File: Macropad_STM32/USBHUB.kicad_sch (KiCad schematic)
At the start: 14 parts, among them U2 CY7C65632-28LTXCT, U4 USBLC6-2SC6, Y1 12MHz

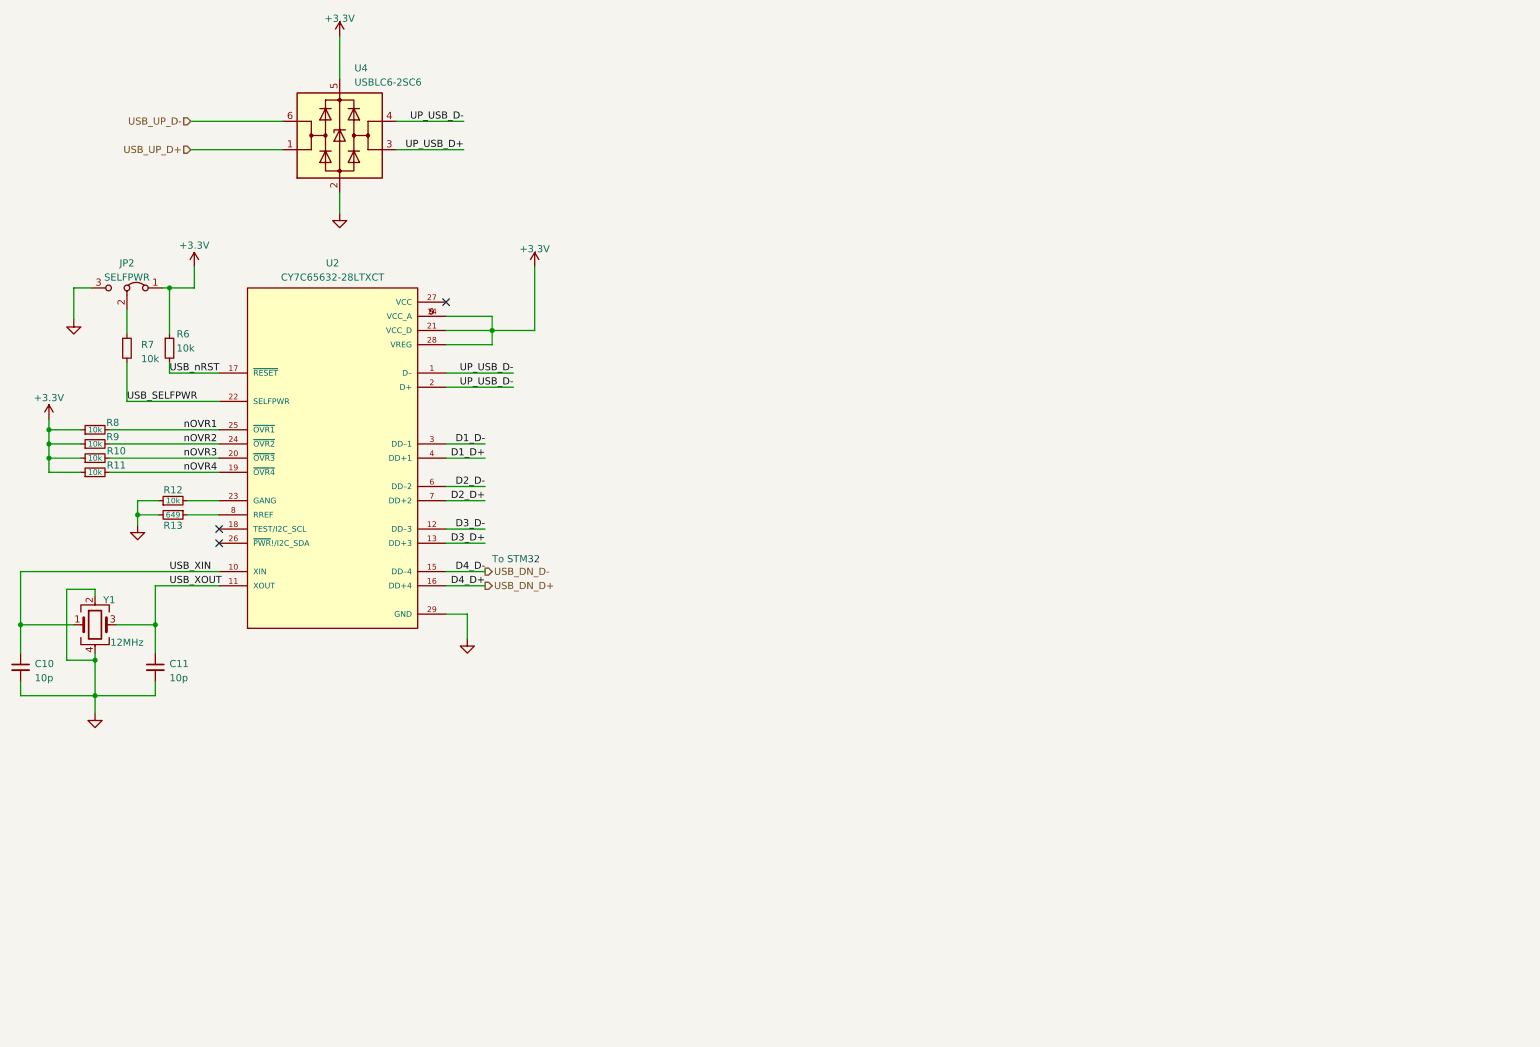
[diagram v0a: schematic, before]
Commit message: USB Hub & Jtag connectors added Todo: - Keypad matrix - Rotary encoders - PCB
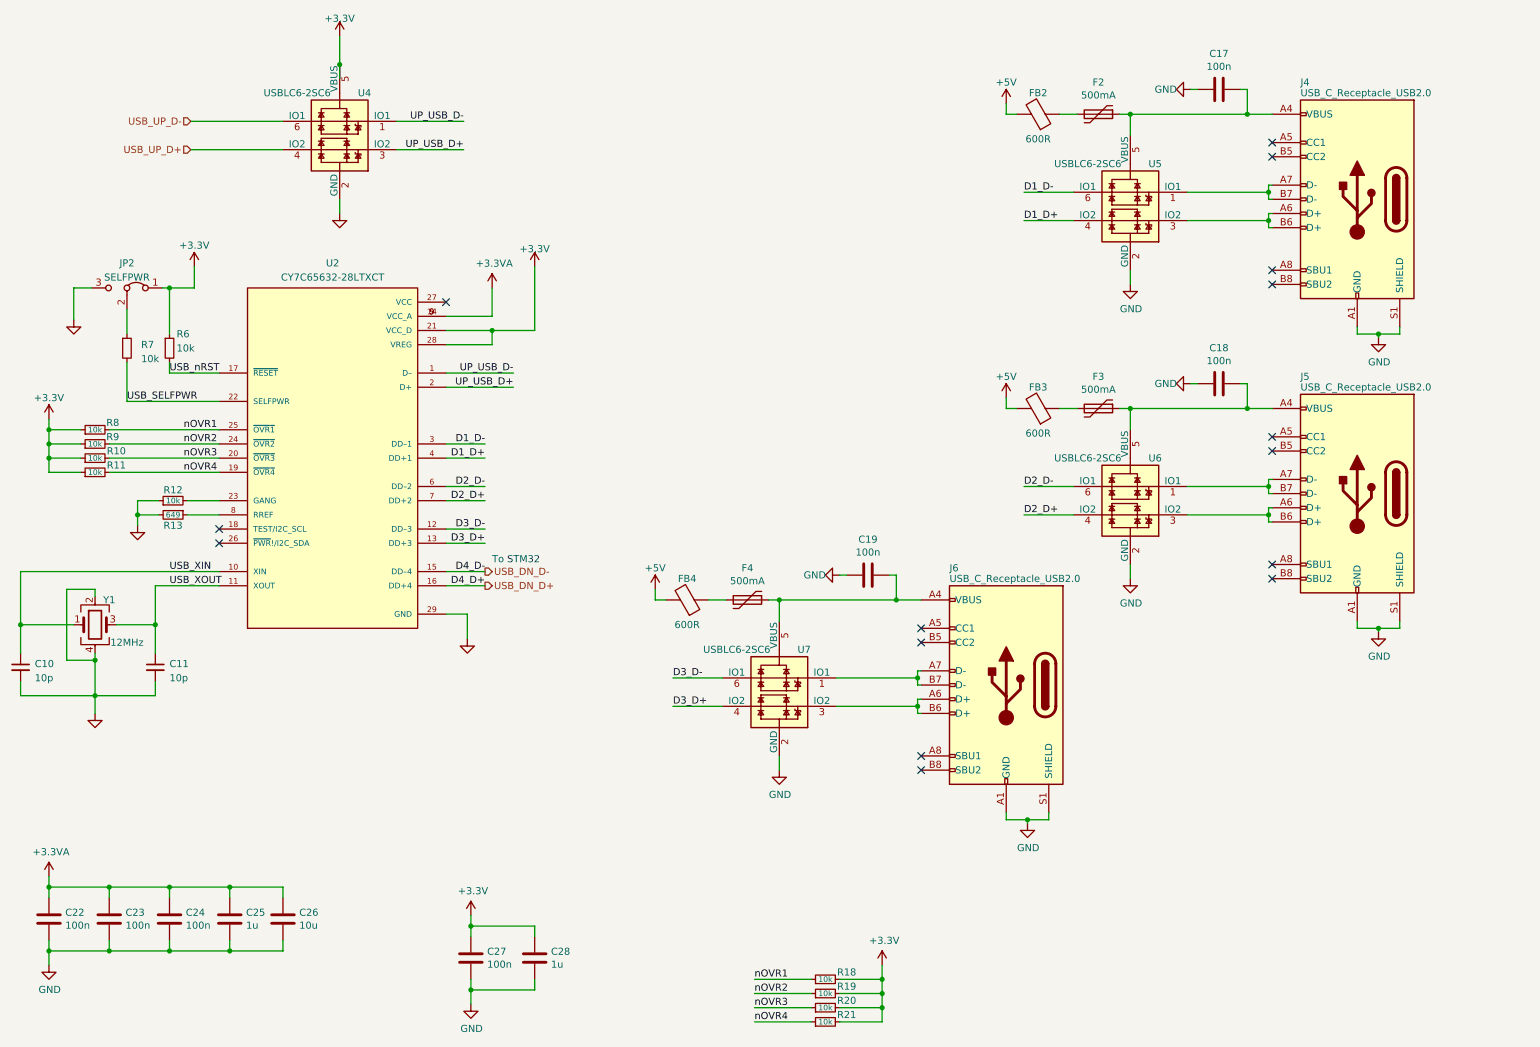
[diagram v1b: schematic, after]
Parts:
- removed U4: USBLC6-2SC6, Package_TO_SOT_SMD:SOT-23-6, symbol Power_Protection:USBLC6-2SC6
- added C17, C18, C19, C22, C23, C24, C27: 100n, Capacitor_SMD:C_0603_1608Metric, symbol Device:C
- added C25, C28: 1u, Capacitor_SMD:C_0603_1608Metric, symbol Device:C
- added C26: 10u, Capacitor_SMD:C_0603_1608Metric, symbol Device:C
- added F2, F3, F4: 500mA, josh-passives-smt:Fuse_0805_2012Metric, symbol Device:Polyfuse
- added FB2, FB3, FB4: 600R, josh-passives-smt:Ferrite_Bead_0603, symbol Hub16-rescue:Ferrite_Bead_PWR-josh-passive
- added J4, J5, J6: USB_C_Receptacle_USB2.0, Connector_USB:USB_C_Receptacle_HRO_TYPE-C-31-M-12, symbol Hub16-rescue:USB_C_Receptacle_USB2.0-Connector
- added R18, R19, R20, R21: 10k, symbol Device:R_Small
- added U4, U5, U6, U7: USBLC6-2SC6, Package_TO_SOT_SMD:SOT-23-6, symbol Hub16-rescue:USBLC6-2SC6-josh-ic
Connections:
- net +3.3V: now also U4.5 (VBUS); no longer U2.14 (VCC_A), U2.5 (VCC_A), U2.9 (VCC_A)
- net D1_D+: now also U5.4 (IO2)
- net D1_D-: now also U5.6 (IO1)
- net D2_D+: now also U6.4 (IO2)
- net D2_D-: now also U6.6 (IO1)
- net D3_D+: now also U7.4 (IO2)
- net D3_D-: now also U7.6 (IO1)
- net GND: now also C17.2, C18.2, C19.2, C22.2, C23.2, C24.2, C25.2, C26.2, C27.2, C28.2, J4.A1 (GND), J4.A12 (GND), J4.B1 (GND), J4.B12 (GND), J4.S1 (SHIELD), J5.A1 (GND), J5.A12 (GND), J5.B1 (GND), J5.B12 (GND), J5.S1 (SHIELD), J6.A1 (GND), J6.A12 (GND), J6.B1 (GND), J6.B12 (GND), J6.S1 (SHIELD), U4.2 (GND), U5.2 (GND), U6.2 (GND), U7.2 (GND)
- net UP_USB_D+: now also U2.2 (D+), U4.3 (IO2)
- net UP_USB_D-: now also U4.1 (IO1); no longer U2.2 (D+)
- net USB_UP_D+: now also U4.4 (IO2)
- net USB_UP_D-: now also U4.6 (IO1)
- net nOVR1: now also R18.1
- net nOVR2: now also R19.1
- net nOVR3: now also R20.1
- net nOVR4: now also R21.1
- new net: F4.2, FB4.1
- new net: C19.1, F4.1, J6.A4 (VBUS), J6.A9 (VBUS), J6.B4 (VBUS), J6.B9 (VBUS), U7.5 (VBUS)
- new net: F2.2, FB2.1
- new net: F3.2, FB3.1
- new net: J5.A7 (D-), J5.B7 (D-), U6.1 (IO1)
- new net: J5.A6 (D+), J5.B6 (D+), U6.3 (IO2)
- new net: C18.1, F3.1, J5.A4 (VBUS), J5.A9 (VBUS), J5.B4 (VBUS), J5.B9 (VBUS), U6.5 (VBUS)
- new net: C17.1, F2.1, J4.A4 (VBUS), J4.A9 (VBUS), J4.B4 (VBUS), J4.B9 (VBUS), U5.5 (VBUS)
- new net: J6.A6 (D+), J6.B6 (D+), U7.3 (IO2)
- new net: J6.A7 (D-), J6.B7 (D-), U7.1 (IO1)
- new net: J4.A7 (D-), J4.B7 (D-), U5.1 (IO1)
- new net: J4.A6 (D+), J4.B6 (D+), U5.3 (IO2)
- new net +3.3VA: C22.1, C23.1, C24.1, C25.1, C26.1, U2.14 (VCC_A), U2.5 (VCC_A), U2.9 (VCC_A)
- new net +3V3: C27.1, C28.1, R18.2, R19.2, R20.2, R21.2
- new net +5V: FB2.2, FB3.2, FB4.2
- no-connect marks 3 -> 15

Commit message: Finished main schematic (excl. matrix)
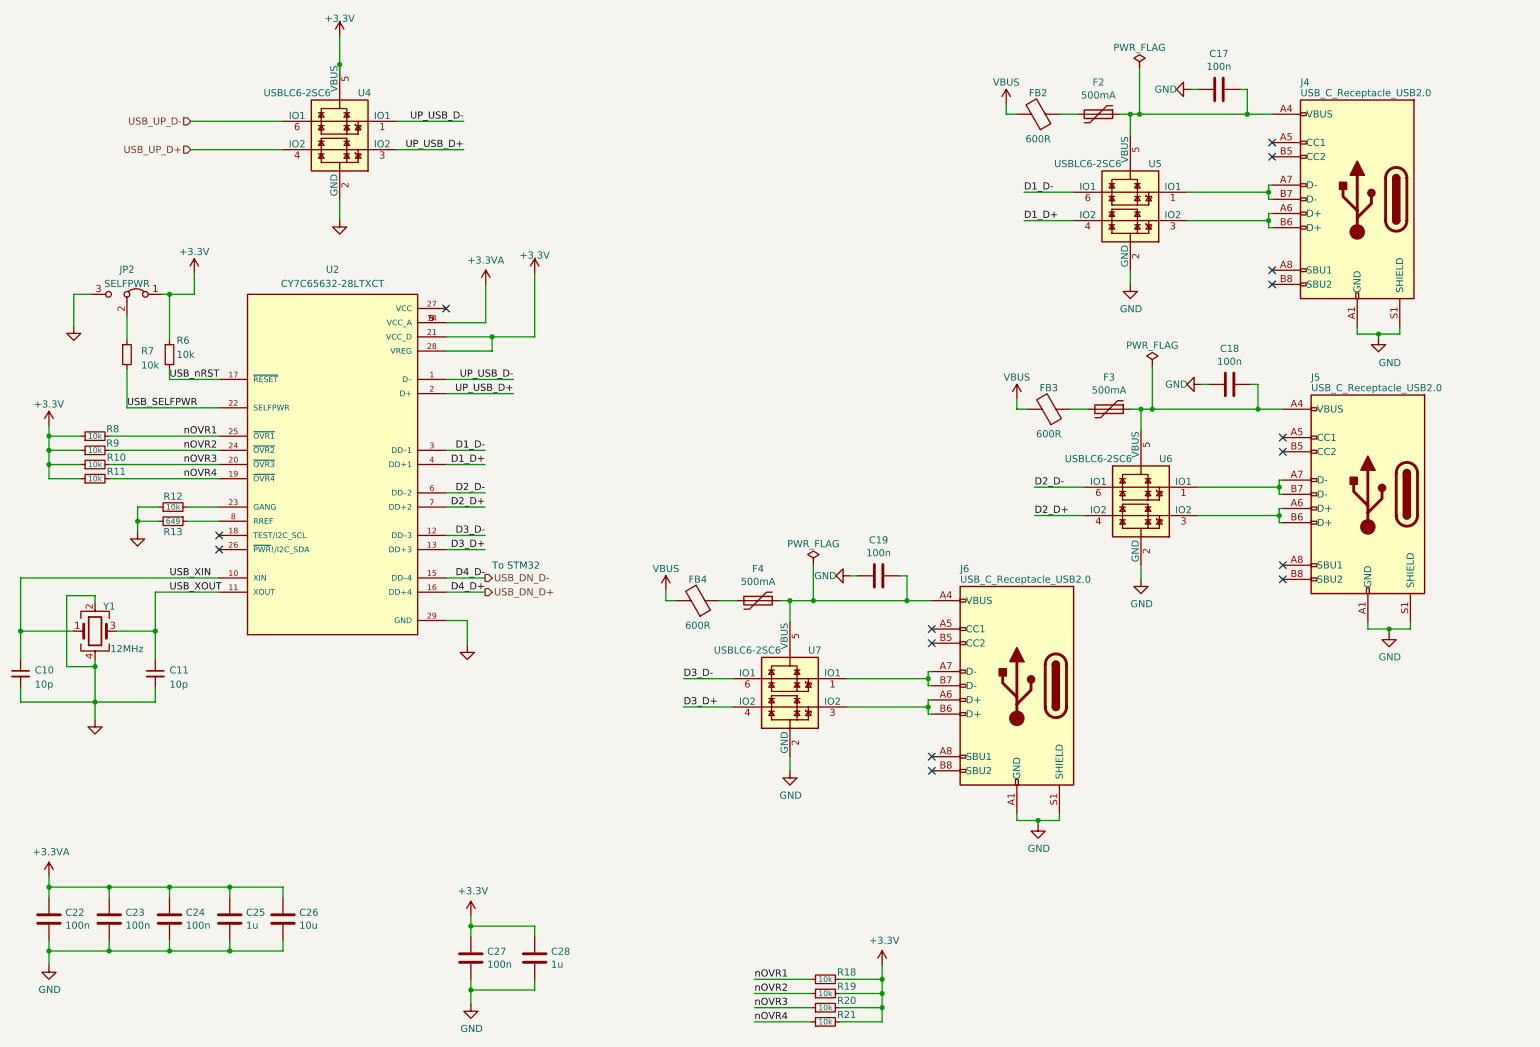
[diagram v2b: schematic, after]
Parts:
- C10, C11: footprint (none) -> Capacitor_SMD:C_0805_2012Metric_Pad1.18x1.45mm_HandSolder
- C17, C18, C19, C22, C23, C24, C25, C26, C27, C28: footprint Capacitor_SMD:C_0603_1608Metric -> Capacitor_SMD:C_0805_2012Metric_Pad1.18x1.45mm_HandSolder
- F2, F3, F4: footprint josh-passives-smt:Fuse_0805_2012Metric -> Fuse:Fuse_1206_3216Metric_Pad1.42x1.75mm_HandSolder
- FB2, FB3, FB4: footprint josh-passives-smt:Ferrite_Bead_0603 -> Fuse:Fuse_0805_2012Metric_Pad1.15x1.40mm_HandSolder
- JP2: footprint (none) -> Connector_PinHeader_2.54mm:PinHeader_1x03_P2.54mm_Vertical
- R10, R11, R12, R13, R18, R19, R20, R21, R6, R7, R8, R9: footprint (none) -> Resistor_SMD:R_0805_2012Metric_Pad1.20x1.40mm_HandSolder
- U2: footprint CY7C65632-28LTXCT:QFN50P500X500X80-29N -> KicadFootprints:QFN50P500X500X80-29N
- Y1: footprint (none) -> Crystal:Crystal_SMD_3225-4Pin_3.2x2.5mm_HandSoldering
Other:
- moved on the sheet: C10, C11, C18, C19, F3, F4, FB3, FB4, J5, J6, JP2, R10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

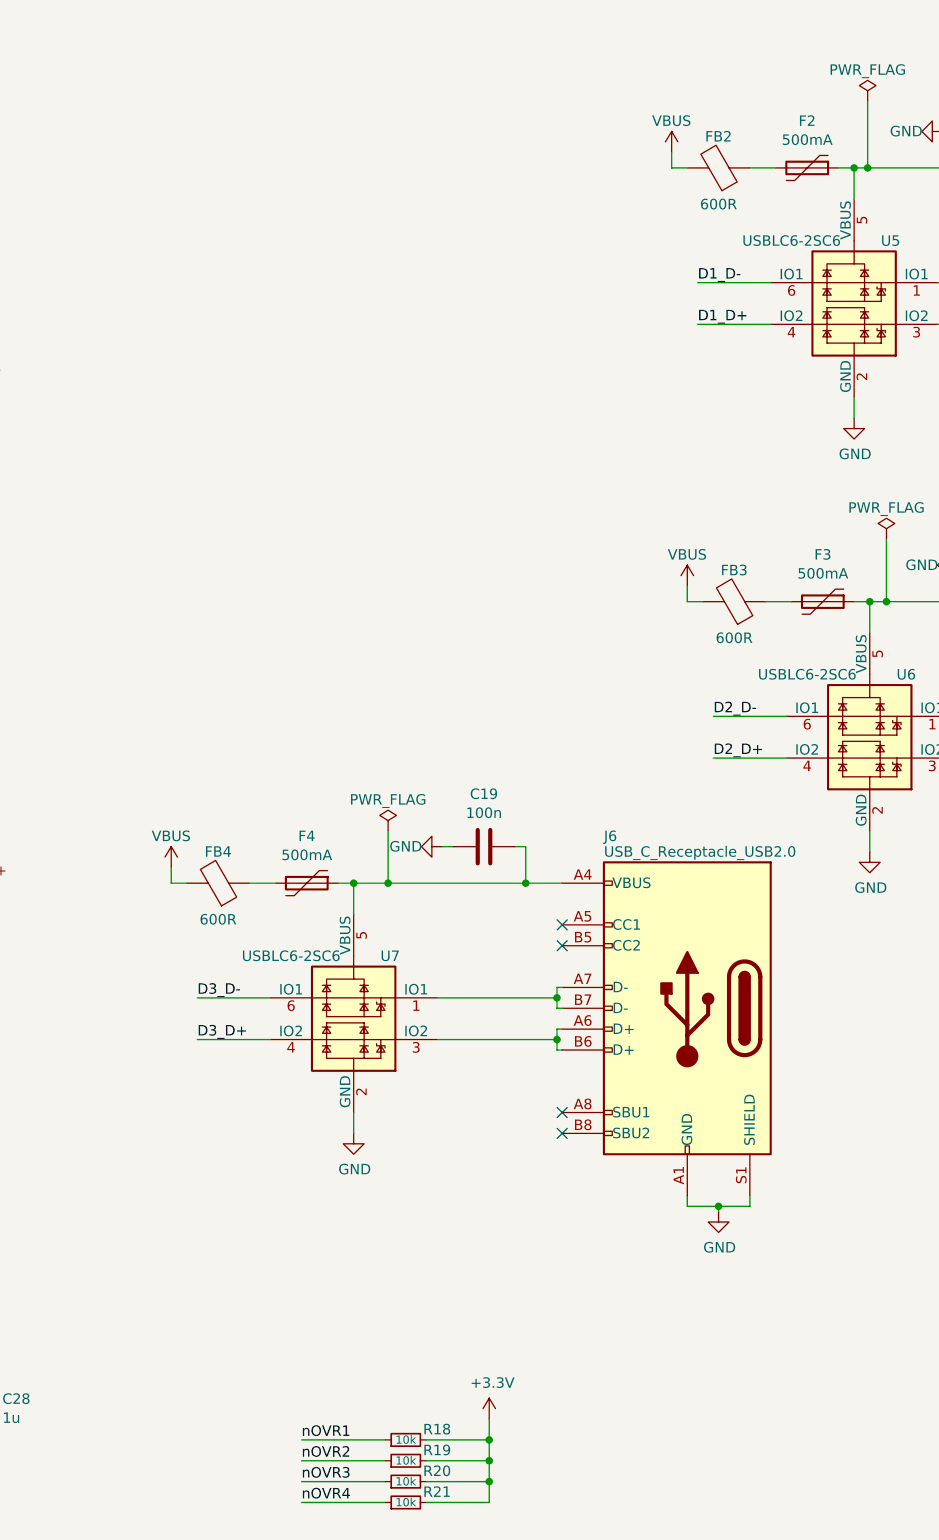
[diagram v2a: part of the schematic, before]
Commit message: Finished PCB layout, TODO: traces
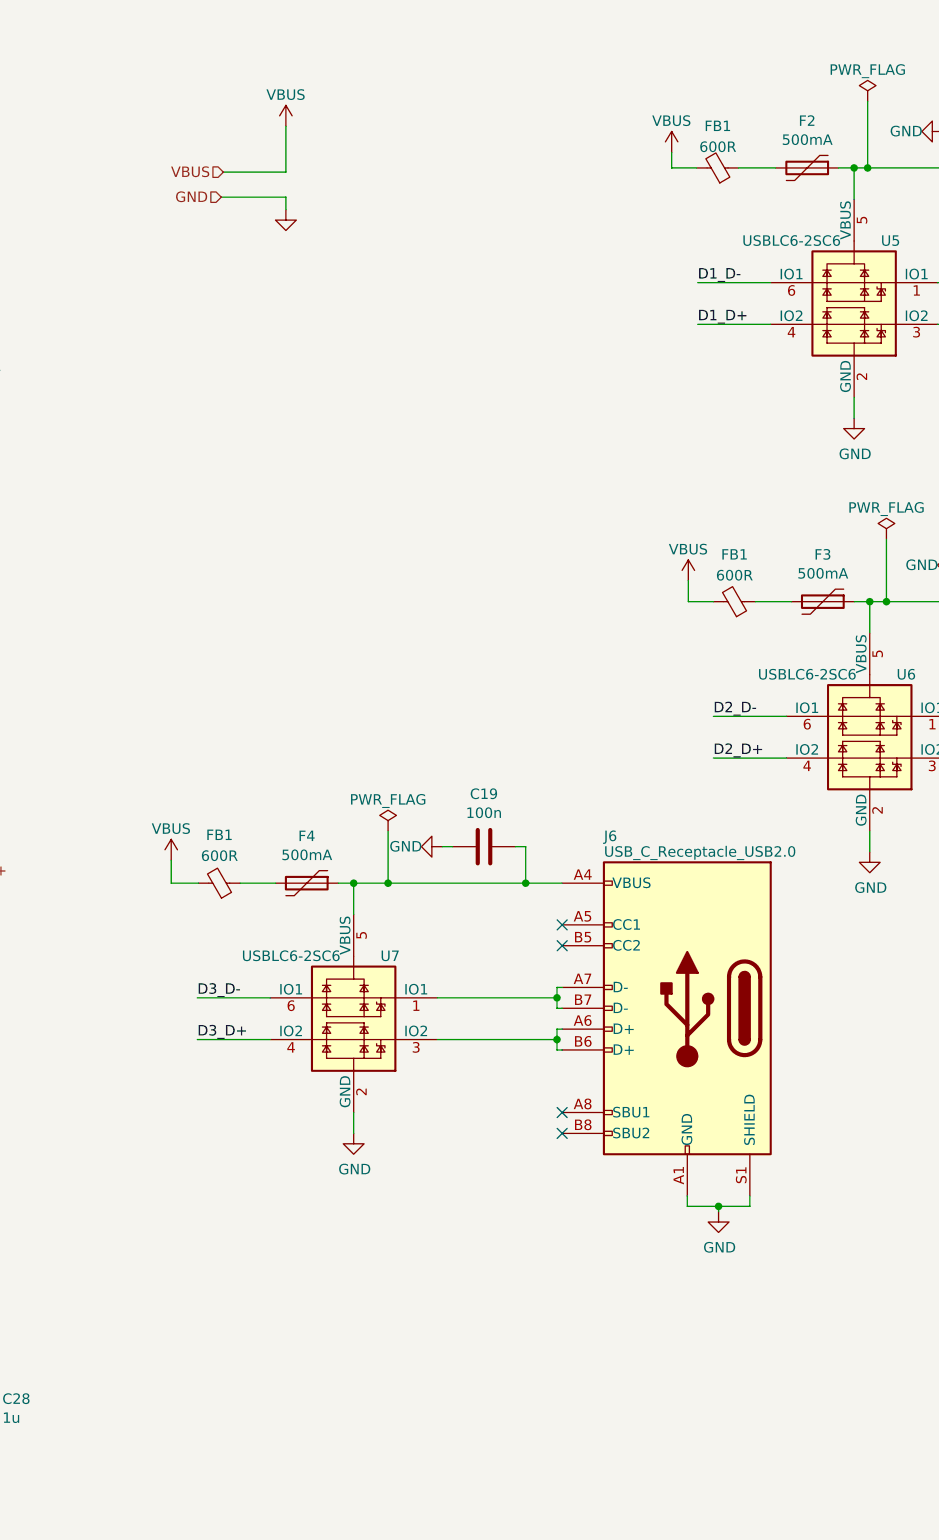
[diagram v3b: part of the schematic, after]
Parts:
- removed FB2, FB3, FB4: 600R, Fuse:Fuse_0805_2012Metric_Pad1.15x1.40mm_HandSolder, symbol Hub16-rescue:Ferrite_Bead_PWR-josh-passive
- removed R18, R19, R20, R21: 10k, Resistor_SMD:R_0805_2012Metric_Pad1.20x1.40mm_HandSolder, symbol Device:R_Small
- added FB1 (x3): 600R, Fuse:Fuse_0805_2012Metric_Pad1.15x1.40mm_HandSolder, symbol Device:FerriteBead_Small
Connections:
- net +5V: now also FB1.2, FB1.2, FB1.2
- net at F4.2: now also FB1.1
- net at F2.2: now also FB1.1
- net at F3.2: now also FB1.1
